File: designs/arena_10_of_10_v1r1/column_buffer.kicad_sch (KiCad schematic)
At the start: 32 parts

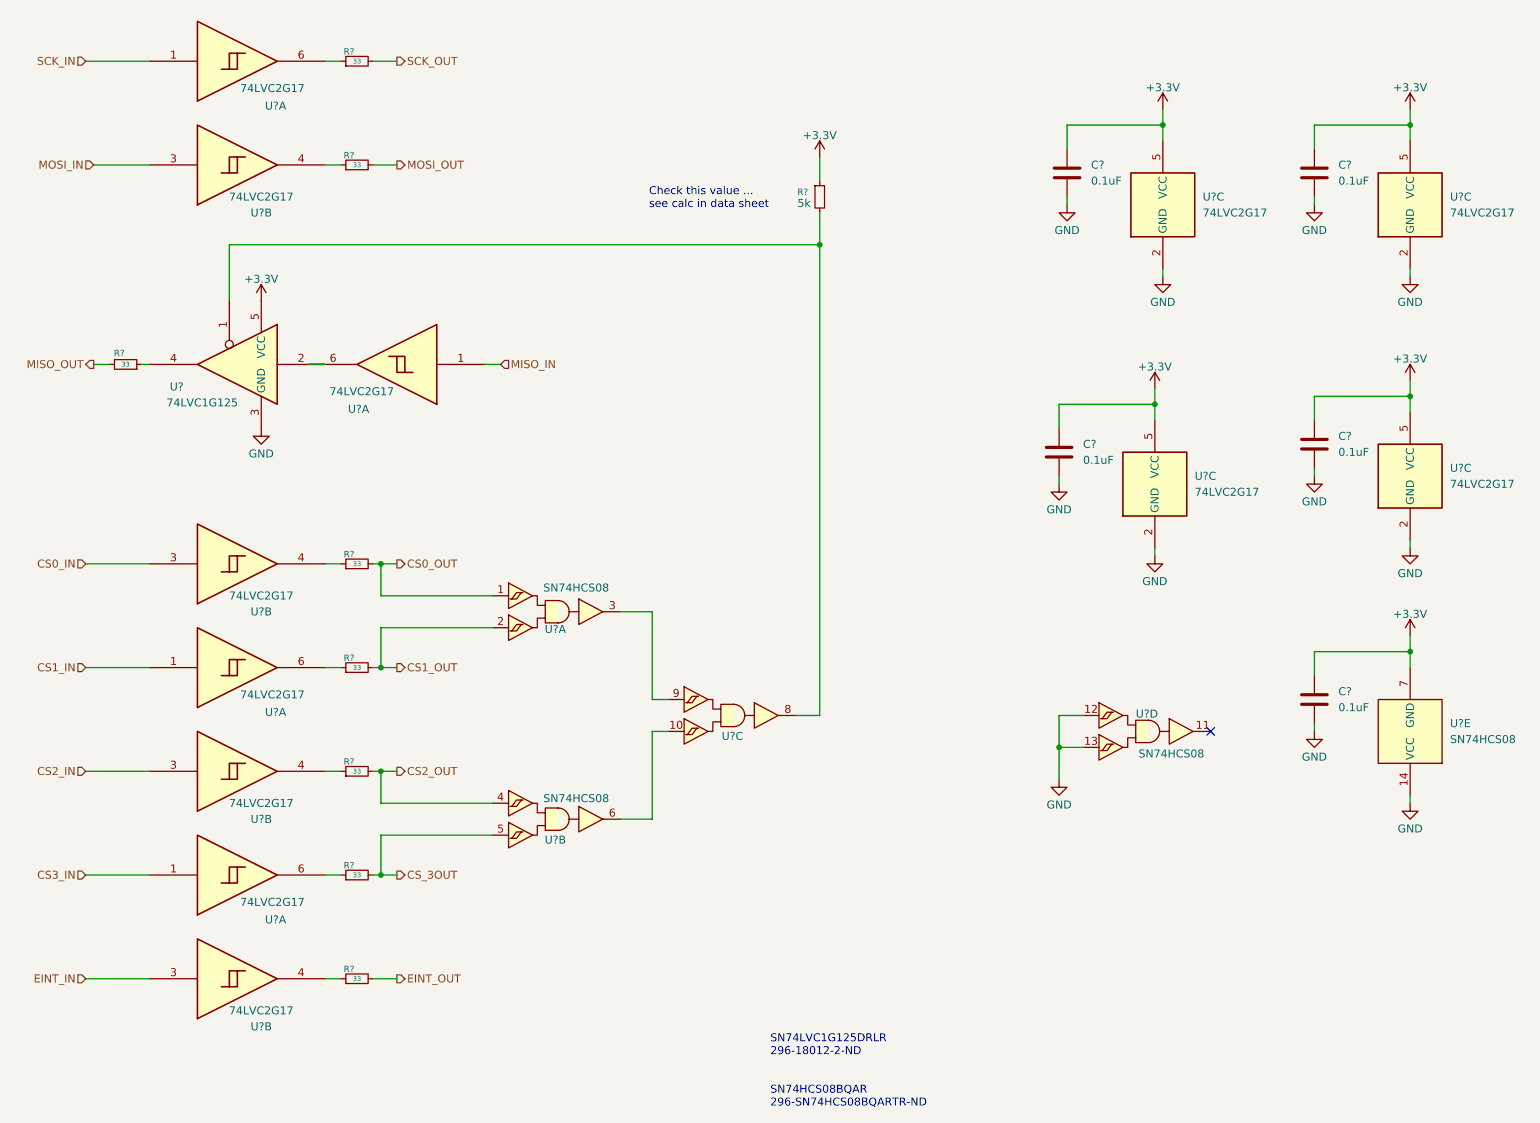
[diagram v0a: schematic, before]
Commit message: Re-worked MISO handling and analog input circuit.
Modified so that MISO isolation circuits are in fan out section and
are such that they will be placed close to the teensy.  Modified the
analog input circuit so that the teensy MCU analog inputs are used in
conjuction with a level shifting circuit.
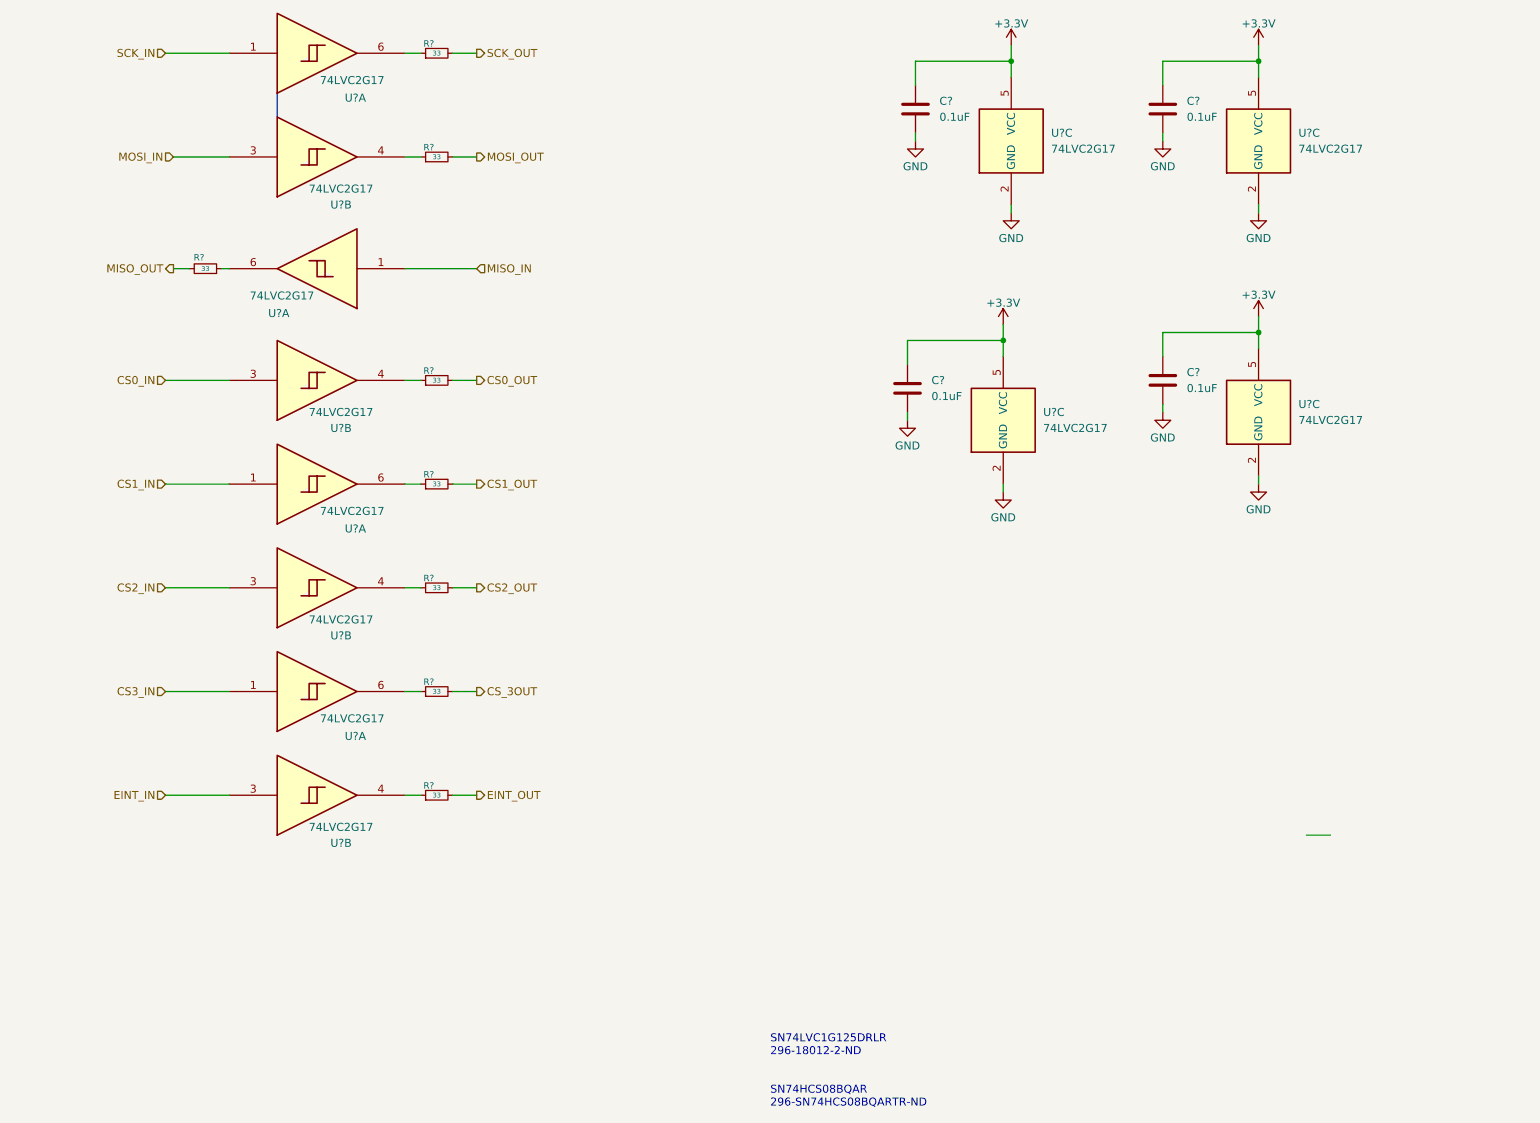
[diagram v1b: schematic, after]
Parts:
- removed C?: 0.1uF, Capacitor_SMD:C_0402_1005Metric, symbol Device:C
- removed R?: 5k, symbol Device:R_Small
- removed U? (x5): SN74HCS08, symbol SN74HCS08:SN74HCS08
- removed U?: 74LVC1G125, symbol 74xGxx:74LVC1G125
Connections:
- net at U?.6: now also R?.1
- no-connect marks 1 -> 0
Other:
- note removed: "Check this value ... see calc in data sheet"
- moved on the sheet: C?, R?, U?A, U?B, U?C
